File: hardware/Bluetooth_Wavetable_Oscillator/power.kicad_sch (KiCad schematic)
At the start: 10 parts, among them J1 AWHW2 10G-0202, U1 L7805

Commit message: add audio test files
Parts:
- C1, C4, C5, C6: footprint (none) -> Capacitor_THT:C_Disc_D5.0mm_W2.5mm_P5.00mm
- C2, C3: footprint (none) -> Capacitor_THT:CP_Radial_D5.0mm_P2.50mm
- J1: footprint (none) -> 10_pin_eurorack_connector:10_pin_eurorack_connector
- U1: footprint (none) -> Package_TO_SOT_THT:TO-220-3_Horizontal_TabDown
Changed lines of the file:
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@@
 			)
 		)
-		(property "Footprint" ""
+		(property "Footprint" "Capacitor_THT:CP_Radial_D5.0mm_P2.50mm"
 			(at 103.8352 78.74 0)
 			(effects
@@
 			)
 		)
-		(property "Footprint" ""
+		(property "Footprint" "Capacitor_THT:CP_Radial_D5.0mm_P2.50mm"
 			(at 103.8352 63.5 0)
 			(effects
@@
 			)
 		)
-		(property "Footprint" ""
+		(property "Footprint" "Capacitor_THT:C_Disc_D5.0mm_W2.5mm_P5.00mm"
 			(at 121.6152 63.5 0)
 			(effects
@@
 			)
 		)
-		(property "Footprint" ""
+		(property "Footprint" "10_pin_eurorack_connector:10_pin_eurorack_connector"
 			(at 64.77 78.74 0)
 			(effects
@@
 			)
 		)
-		(property "Footprint" ""
+		(property "Footprint" "Capacitor_THT:C_Disc_D5.0mm_W2.5mm_P5.00mm"
 			(at 82.2452 132.08 0)
 			(effects
@@
 			)
 		)
-		(property "Footprint" ""
+		(property "Footprint" "Capacitor_THT:C_Disc_D5.0mm_W2.5mm_P5.00mm"
 			(at 121.6152 78.74 0)
 			(effects
@@
 			)
 		)
-		(property "Footprint" ""
+		(property "Footprint" "Capacitor_THT:C_Disc_D5.0mm_W2.5mm_P5.00mm"
 			(at 106.3752 132.08 0)
 			(effects
@@
 			)
 		)
-		(property "Footprint" ""
+		(property "Footprint" "Package_TO_SOT_THT:TO-220-3_Horizontal_TabDown"
 			(at 94.615 128.27 0)
 			(effects

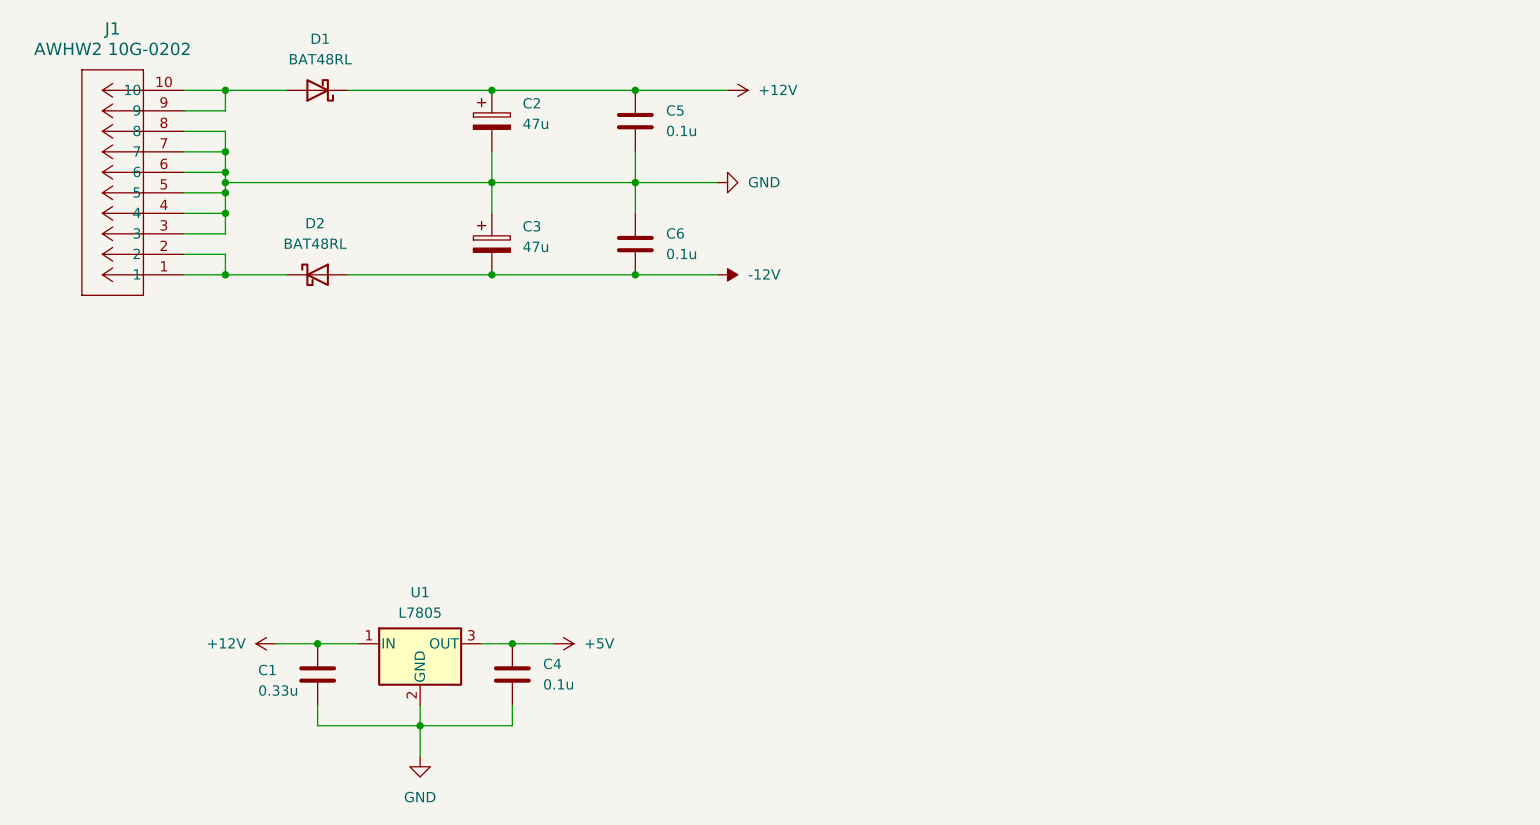
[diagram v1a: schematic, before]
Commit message: add bth components, add component values, update SPI pins, change disp power supply to 5V
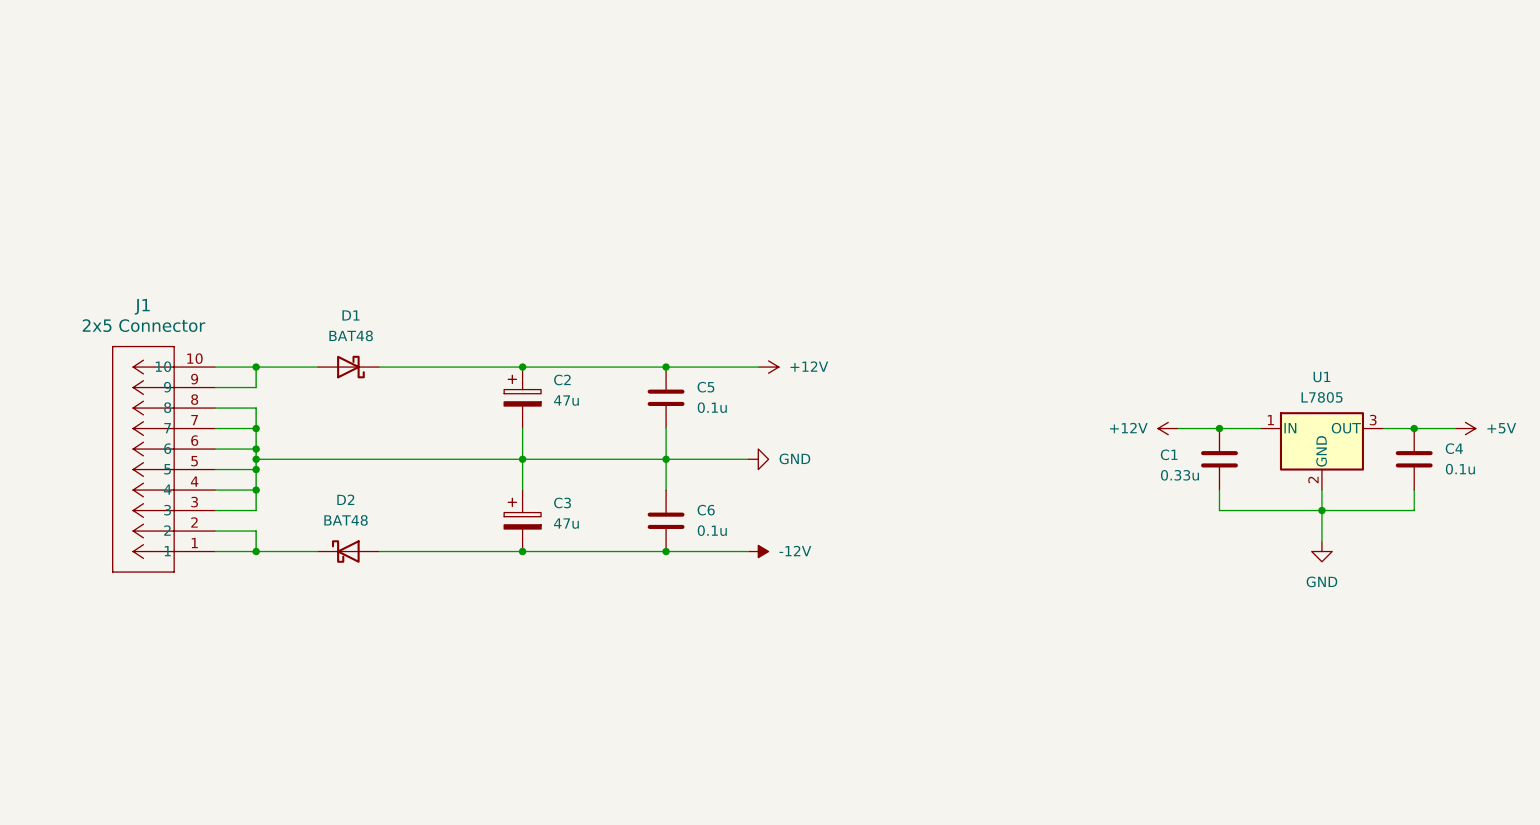
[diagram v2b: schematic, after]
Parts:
- D1, D2: value BAT48RL -> BAT48
- J1: value AWHW2 10G-0202 -> 2x5 Connector
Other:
- moved on the sheet: C1, C2, C3, C4, C5, C6, D1, D2, J1, U1

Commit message: update shematic, PCB and footprints
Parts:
- D1, D2: footprint Diode_THT:D_DO-35_SOD27_P7.62mm_Horizontal -> Diode_THT:D_DO-35_SOD27_P2.54mm_Vertical_KathodeUp
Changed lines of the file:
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@@
 			)
 		)
-		(property "Footprint" "Diode_THT:D_DO-35_SOD27_P7.62mm_Horizontal"
+		(property "Footprint" "Diode_THT:D_DO-35_SOD27_P2.54mm_Vertical_KathodeUp"
 			(at 85.09 117.475 0)
 			(effects
@@
 			)
 		)
-		(property "Footprint" "Diode_THT:D_DO-35_SOD27_P7.62mm_Horizontal"
+		(property "Footprint" "Diode_THT:D_DO-35_SOD27_P2.54mm_Vertical_KathodeUp"
 			(at 85.09 85.725 0)
 			(effects
